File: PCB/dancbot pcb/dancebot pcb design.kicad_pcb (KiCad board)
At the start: 2 copper layers, 27 parts, among them J1 ESP32-PICO-KIT-V4.1, J2 Voltage Regulator, J4 Pins, J6 Conn_01x04_Socket, J7 Conn_01x04_Socket, Q1 PMOS, Q2 PMOS, Q3 2N3904, Q5 PMOS, SW1 SP switch, SW2 SW_SPST

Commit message: Layout Connections Revision 3
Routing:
- net +5V: track 97.9 -> 92.1 mm
- net GND1: track 3.71 -> 7.32 mm, vias 0 -> 2
- net SM4: track 18.5 -> 19.5 mm
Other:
- board outline added: 62.5 x 55 mm
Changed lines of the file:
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@@
     )
   )
-  (gr_rect (start 182 56) (end 251 121)
-    (stroke (width 0.2) (type default)) (fill none) (layer "F.Cu"))
+  (gr_rect (start 182.5 57.5) (end 245 112.5)
+    (stroke (width 0.1) (type default)) (fill none) (layer "Edge.Cuts"))
   (segment (start 197.92 63) (end 192.92 68) (width 0.25) (layer "F.Cu") (net 3))
   (segment (start 223.885 60.635) (end 224.73 61.48) (width 0.25) (layer "F.Cu") (net 3))
@@
   (segment (start 197.31104 98.5) (end 200.66 101.84896) (width 0.25) (layer "F.Cu") (net 6))
   (segment (start 237.5 62.46) (end 242.5 67.46) (width 0.25) (layer "F.Cu") (net 6))
-  (segment (start 192 101) (end 194.5 98.5) (width 0.25) (layer "F.Cu") (net 6))
   (segment (start 237.738 91.468) (end 237.738 95) (width 0.25) (layer "F.Cu") (net 6))
   (segment (start 242.5 67.46) (end 242.5 95) (width 0.25) (layer "F.Cu") (net 6))
@@
   (segment (start 242.5 95) (end 237.738 95) (width 0.25) (layer "F.Cu") (net 6))
   (segment (start 237.738 95.002) (end 236.22 96.52) (width 0.25) (layer "F.Cu") (net 6))
-  (segment (start 194.5 98.5) (end 196.71 98.5) (width 0.25) (layer "F.Cu") (net 6))
   (segment (start 200.66 103.23104) (end 203.10896 105.68) (width 0.25) (layer "F.Cu") (net 6))
   (segment (start 206.74 105.68) (end 203.71 105.68) (width 0.25) (layer "F.Cu") (net 6))
@@
   (segment (start 215.9 96.52) (end 208.28 104.14) (width 0.25) (layer "B.Cu") (net 6))
   (segment (start 236.22 96.52) (end 215.9 96.52) (width 0.25) (layer "B.Cu") (net 6))
-  (segment (start 217.418 105.387) (end 215.9 106.905) (width 0.25) (layer "F.Cu") (net 7))
-  (segment (start 217.418 91.468) (end 217.418 105.387) (width 0.25) (layer "F.Cu") (net 7))
-  (segment (start 219.958 91.468) (end 219.958 105.702) (width 0.25) (layer "F.Cu") (net 8))
-  (segment (start 219.958 105.702) (end 218.44 107.22) (width 0.25) (layer "F.Cu") (net 8))
+  (segment (start 215.9 92.986) (end 215.9 106.905) (width 0.25) (layer "F.Cu") (net 7))
+  (segment (start 217.418 91.468) (end 215.9 92.986) (width 0.25) (layer "F.Cu") (net 7))
+  (segment (start 219.958 91.468) (end 218.44 92.986) (width 0.25) (layer "F.Cu") (net 8))
+  (segment (start 218.44 92.986) (end 218.44 107.22) (width 0.25) (layer "F.Cu") (net 8))
   (segment (start 214.878 91.468) (end 213.36 92.986) (width 0.25) (layer "F.Cu") (net 9))
   (segment (start 213.36 92.986) (end 213.36 106.905) (width 0.25) (layer "F.Cu") (net 9))
-  (segment (start 220.98 92.986) (end 220.98 106.68) (width 0.25) (layer "F.Cu") (net 10))
-  (segment (start 221.3 107) (end 223.52 107) (width 0.25) (layer "F.Cu") (net 10))
-  (segment (start 220.98 106.68) (end 221.3 107) (width 0.25) (layer "F.Cu") (net 10))
-  (segment (start 222.498 91.468) (end 220.98 92.986) (width 0.25) (layer "F.Cu") (net 10))
+  (segment (start 220 106) (end 221 107) (width 0.25) (layer "F.Cu") (net 10))
+  (segment (start 221 107) (end 223.52 107) (width 0.25) (layer "F.Cu") (net 10))
+  (segment (start 220 93.966) (end 220 106) (width 0.25) (layer "F.Cu") (net 10))
+  (segment (start 222.498 91.468) (end 220 93.966) (width 0.25) (layer "F.Cu") (net 10))
   (segment (start 190 70) (end 185.675 74.325) (width 0.25) (layer "F.Cu") (net 11))
   (segment (start 207.5 107.5) (end 208 107) (width 0.25) (layer "F.Cu") (net 11))
@@
   (segment (start 222.6075 99.6875) (end 223.92 101) (width 0.25) (layer "F.Cu") (net 48))
   (segment (start 193 107.18) (end 196.71 107.18) (width 0.25) (layer "F.Cu") (net 49))
+  (segment (start 223.52 108) (end 225 106.52) (width 0.25) (layer "F.Cu") (net 49))
+  (segment (start 225 106.52) (end 225 106) (width 0.25) (layer "F.Cu") (net 49))
+  (via (at 225 106) (size 0.8) (drill 0.4) (layers "F.Cu" "B.Cu") (net 49))
+  (via (at 225 105) (size 0.8) (drill 0.4) (layers "F.Cu" "B.Cu") (net 49))
+  (segment (start 225 106) (end 225 105) (width 0.25) (layer "B.Cu") (net 49))
   (segment (start 215.486 68) (end 209.798 73.688) (width 0.25) (layer "F.Cu") (net 50))
   (segment (start 217 68) (end 215.486 68) (width 0.25) (layer "F.Cu") (net 50))
@@
     (polygon
       (pts
-        (xy 180 55)
-        (xy 253 55)
-        (xy 253 122)
-        (xy 180 122)
+        (xy 181 56)
+        (xy 181 115)
+        (xy 249 115)
+        (xy 249 56)
       )
     )

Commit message: Layout Connections Revision 4
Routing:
- net GND1: track 7.32 -> 37.2 mm, vias 2 -> 4
- net +5V: track 92.1 -> 88.4 mm
- net VOUT: track 57.1 -> 55.2 mm
- net Net-(R4-Pad1): track 50.3 -> 49.0 mm
- net SM5: track 75.8 -> 75.2 mm

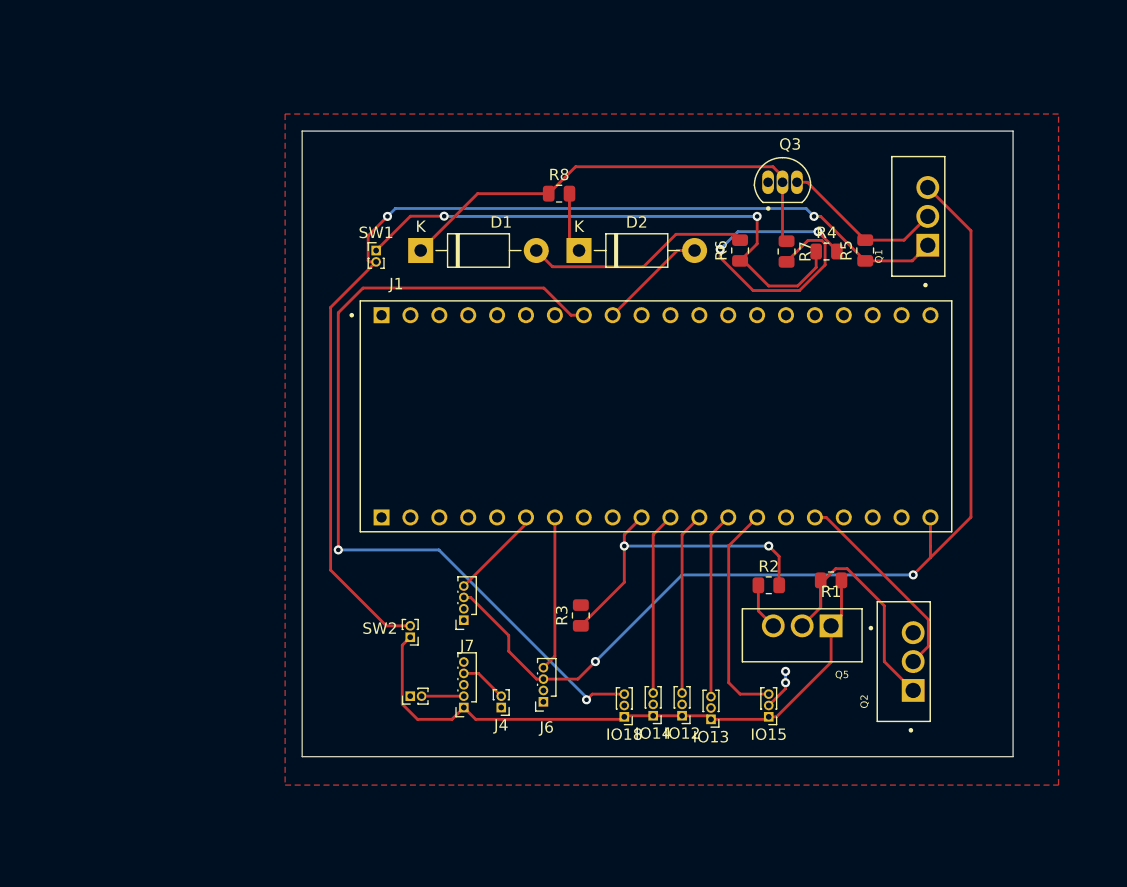
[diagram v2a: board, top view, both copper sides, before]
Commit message: Routing rev5, fixed batt lvl checker, fixed gnd plane
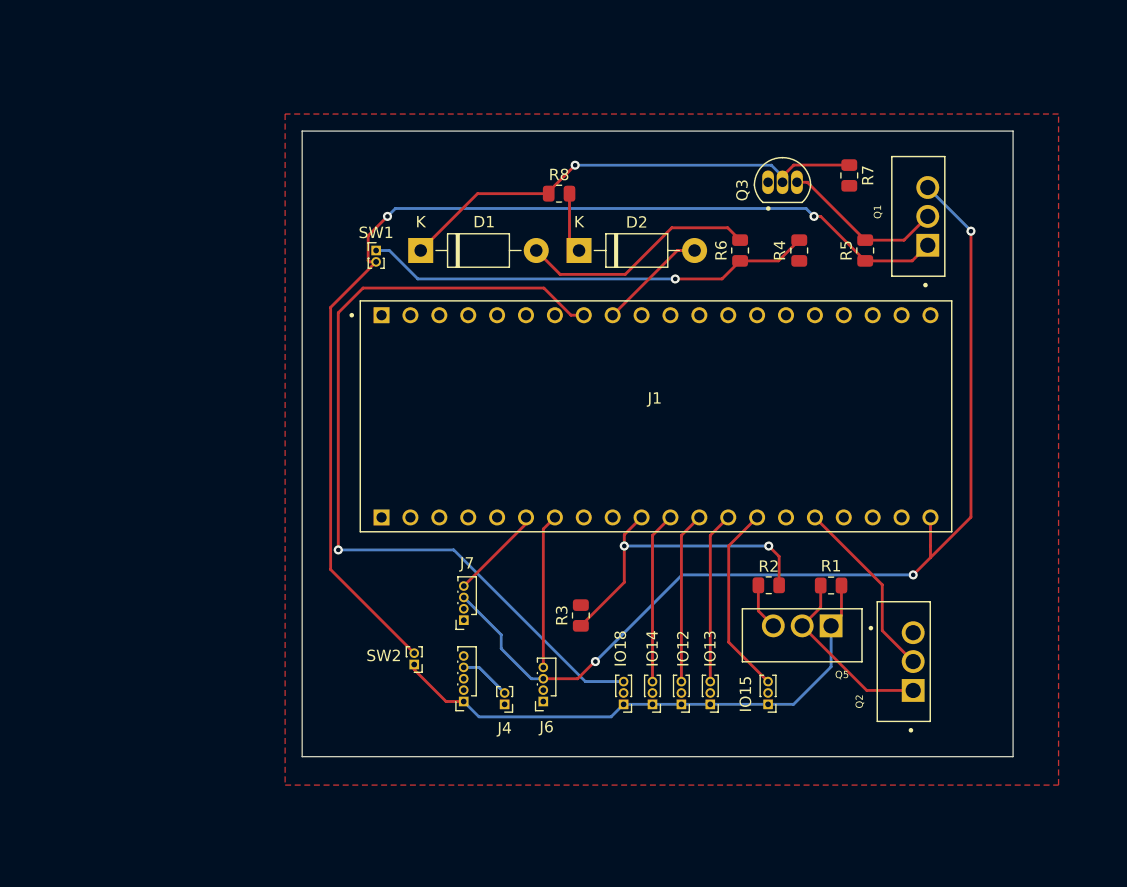
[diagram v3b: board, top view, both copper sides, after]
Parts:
- removed BT1: Battery, Connector_PinHeader_1.00mm:PinHeader_1x02_P1.00mm_Vertical
- moved R7 8.67 mm to (230.6, 61.4)
- moved SW2 2.43 mm to (192.3, 104.4)
- moved R4 2.40 mm to (226.2, 68.0), turned to -90 degrees
- moved IO13 1.32 mm to (218.4, 107.9)
- moved IO15 1.10 mm to (223.5, 107.9)
- moved IO18 1.10 mm to (210.8, 107.9)
- moved IO12 1.01 mm to (215.8, 107.9)
- moved IO14 1.01 mm to (213.3, 107.9)
- moved J2 0.53 mm to (196.7, 107.7)
- moved R1 0.45 mm to (229.0, 97.5)
- moved J4 0.41 mm to (200.3, 107.9)
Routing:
- net GND1: track 37.2 -> 0.00 mm, vias 4 -> 0
- net Net-(R4-Pad1): track 49.0 -> 39.6 mm, vias 2 -> 1
- net Net-(Q2-D): track 22.7 -> 16.3 mm
- net VOUT: track 55.2 -> 49.4 mm
- net SM4: track 19.5 -> 16.9 mm
- net Net-(D1-K): track 41.1 -> 42.8 mm, vias 0 -> 1
- net BATT EN: track 17.9 -> 16.3 mm
- net Net-(Q1-D): track 93.4 -> 94.7 mm
- net SM3: track 16.4 -> 15.1 mm
- net SM5: track 75.2 -> 74.2 mm, vias 2 -> 1
- net Net-(D1-A): track 19.9 -> 20.9 mm
- net SM2: track 16.1 -> 15.1 mm
- net SM1: track 16.1 -> 15.1 mm
- net +5V: track 88.4 -> 88.3 mm, vias 2 -> 3

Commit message: PCB size changed to 62x54mm
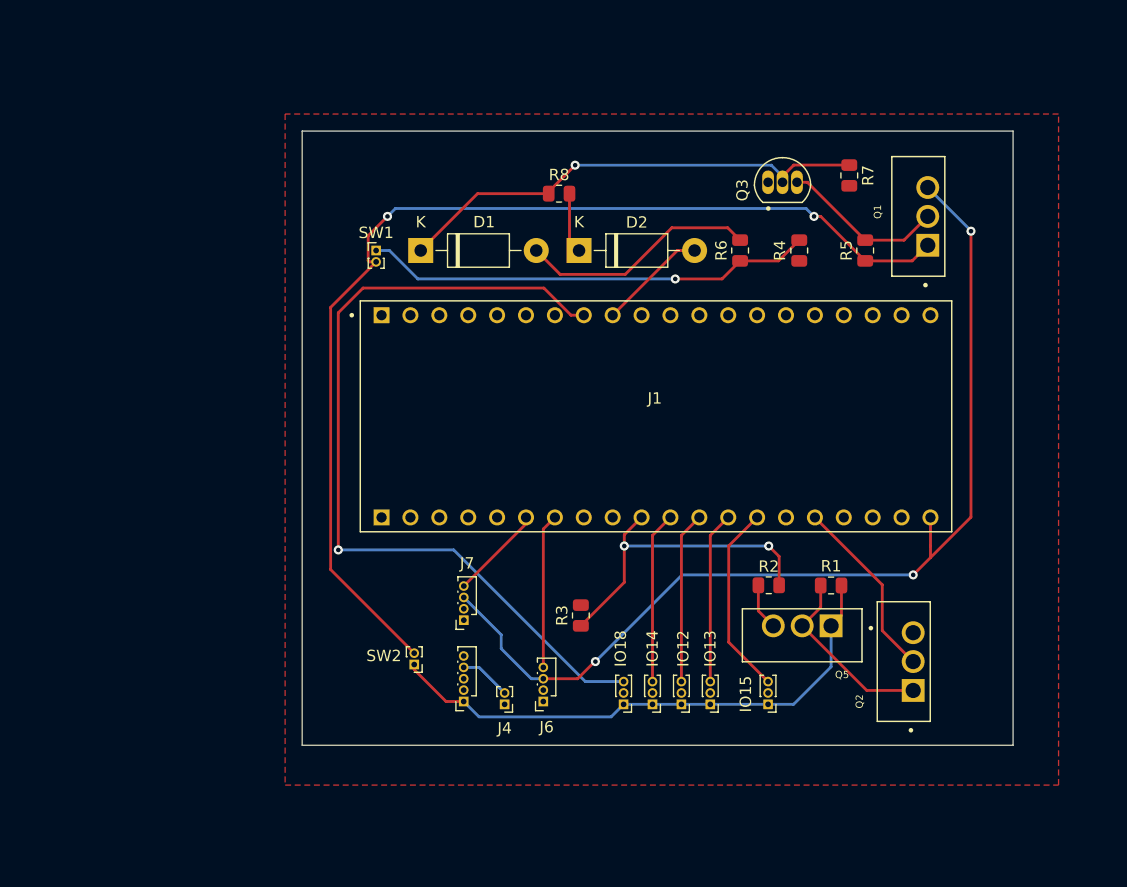
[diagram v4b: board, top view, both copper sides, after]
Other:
- board size 62.5 x 55 mm -> 62.5 x 54 mm
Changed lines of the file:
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@@
     )
   )
-  (gr_rect (start 182.5 57.5) (end 245 112.5)
+  (gr_rect (start 182.5 57.5) (end 245 111.5)
     (stroke (width 0.1) (type default)) (fill none) (layer "Edge.Cuts"))
   (segment (start 224.7 62.03) (end 224.73 62) (width 0.25) (layer "F.Cu") (net 2))

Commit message: Routing rev 6, trace width increased, smd components added
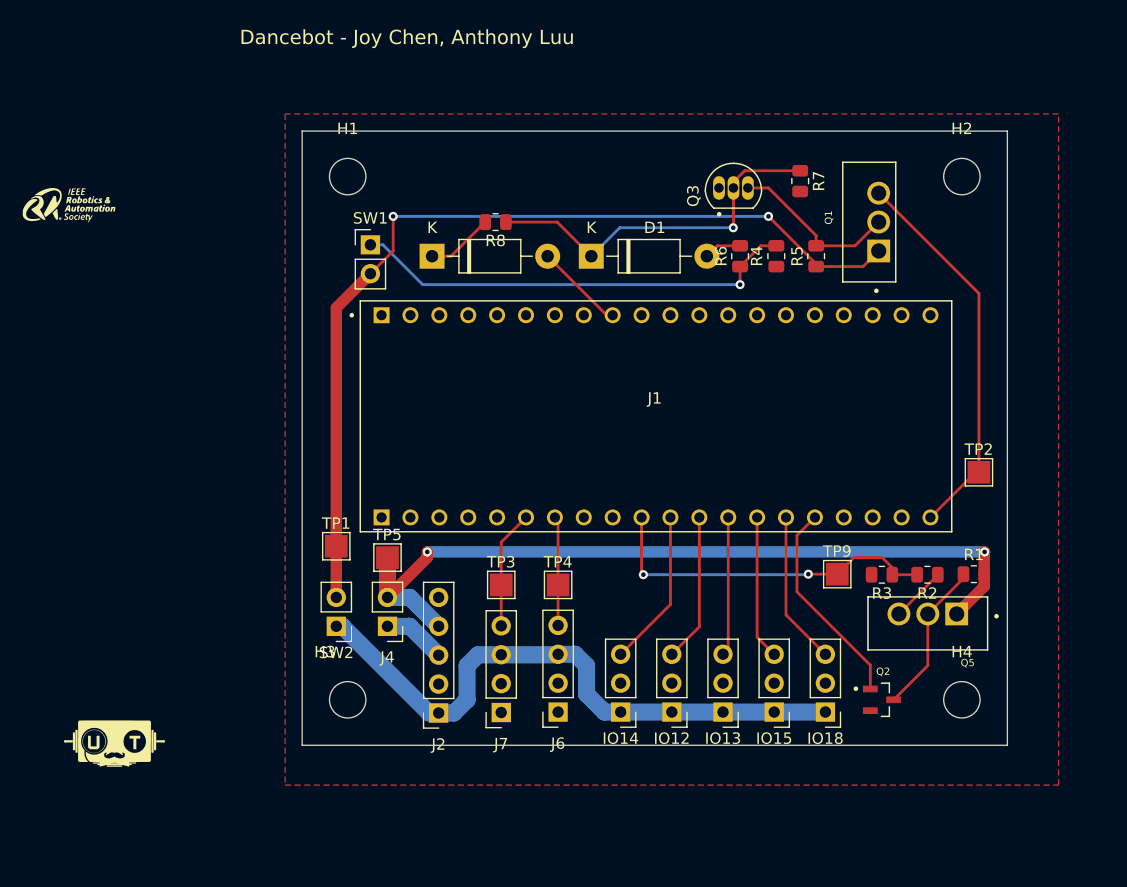
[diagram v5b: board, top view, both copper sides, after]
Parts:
- added G***: LOGO, LOGO, F.Cu at (162.0, 64.0)
- added G***: LOGO, LOGO, F.Cu at (166.0, 111.0)
- added H1: MountingHole, MountingHole:MountingHole_3.2mm_M3, F.Cu at (186.5, 61.5)
- added H2: MountingHole, MountingHole:MountingHole_3.2mm_M3, F.Cu at (240.5, 61.5)
- added H3: MountingHole, MountingHole:MountingHole_3.2mm_M3, F.Cu at (186.5, 107.5)
- added H4: MountingHole, MountingHole:MountingHole_3.2mm_M3, F.Cu at (240.5, 107.5)
- added TP1: TestPoint, TestPoint:TestPoint_Pad_2.0x2.0mm, F.Cu at (185.5, 94.0)
- added TP2: TestPoint, TestPoint:TestPoint_Pad_2.0x2.0mm, F.Cu at (242.0, 87.5)
- added TP3: TestPoint, TestPoint:TestPoint_Pad_2.0x2.0mm, F.Cu at (200.0, 97.4)
- added TP4: TestPoint, TestPoint:TestPoint_Pad_2.0x2.0mm, F.Cu at (205.0, 97.4)
- added TP5: TestPoint, TestPoint:TestPoint_Pad_2.0x2.0mm, F.Cu at (190.0, 95.0)
- added TP9: TestPoint, TestPoint:TestPoint_Pad_2.0x2.0mm, F.Cu at (229.5, 96.5)
- IO12, IO13, IO14, IO15, IO18: footprint Connector_PinHeader_1.00mm:PinHeader_1x03_P1.00mm_Vertical -> Connector_PinHeader_2.54mm:PinHeader_1x03_P2.54mm_Vertical
- J2: footprint Connector_PinSocket_1.00mm:PinSocket_1x05_P1.00mm_Vertical -> Connector_PinSocket_2.54mm:PinSocket_1x05_P2.54mm_Vertical
- J4, SW1, SW2: footprint Connector_PinHeader_1.00mm:PinHeader_1x02_P1.00mm_Vertical -> Connector_PinHeader_2.54mm:PinHeader_1x02_P2.54mm_Vertical
- J6, J7: footprint Connector_PinSocket_1.00mm:PinSocket_1x04_P1.00mm_Vertical -> Connector_PinSocket_2.54mm:PinSocket_1x04_P2.54mm_Vertical
- Q2: value PMOS -> NMOS; footprint dancebot pcb libraries stuff:TO254P1052X465X1989-3 -> Dancebot Footprints:SOT95P237X112-3N
- Q5: footprint dancebot pcb libraries stuff:TO254P1052X465X1989-3 -> Dancebot Footprints:TO254P1052X465X1989-3
- R3: value 10K -> 51k
- moved R3 26.7 mm to (233.5, 96.5), turned to 180 degrees
- moved IO18 17.8 mm to (228.5, 108.6)
- moved D1 15.0 mm to (207.9, 68.5)
- moved R2 14.0 mm to (237.5, 96.5), turned to 180 degrees
- moved D2 12.9 mm to (193.9, 68.5)
- moved R1 12.6 mm to (241.6, 96.5)
- moved J4 12.4 mm to (190.0, 101.0)
- moved Q5 11.1 mm to (240.0, 100.0)
- moved J7 8.76 mm to (200.0, 108.6)
- moved SW2 7.63 mm to (185.5, 101.0)
- moved R8 6.12 mm to (199.5, 65.5), turned to 180 degrees
- moved Q1 4.34 mm to (233.2, 68.0)
- moved Q3 4.34 mm to (220.4, 62.5)
- moved R5 4.34 mm to (227.7, 68.5)
- moved R7 4.34 mm to (226.3, 61.9)
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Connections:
- J1 pad J2_8: SM5 -> unconnected-(J1-IO18-PadJ2_8)
- J1 pad J3_15: unconnected-(J1-IO2-PadJ3_15) -> SM5
- J4 pad 1: GND1 -> Batt GND
- J6 pad 3: +5V -> VOUT
- J7 pad 3: +5V -> VOUT
- Q2 pad 1: Net-(Q2-D) -> BATT EN
- Q2 pad 2: BATT EN -> GND1
- Q2 pad 3: GND1 -> Net-(Q5-G)
- Q5 pad 1: VOUT -> Batt PWR
- Q5 pad 2: Net-(Q2-D) -> Net-(Q5-G)
- R1 pad 1: VOUT -> Batt PWR
- R1 pad 2: Net-(Q2-D) -> Net-(Q5-G)
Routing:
- net Batt PWR: track 4.53 -> 70.0 mm, vias 0 -> 2
- net SM5: track 74.2 -> 13.5 mm, vias 1 -> 0
- net +5V: track 88.3 -> 34.1 mm, vias 3 -> 0
- net Net-(D1-A): track 20.9 -> 3.30 mm
- net Net-(Q2-D): track 16.3 -> 0.00 mm
- net Net-(Q1-D): track 94.7 -> 80.8 mm
- net Net-(Q5-G): track 0.00 -> 13.6 mm
- net Net-(D1-K): track 42.8 -> 33.1 mm
- net Batt GND: track 0.00 -> 5.55 mm
- net VOUT: track 49.4 -> 53.6 mm
- net SM4: track 16.9 -> 12.7 mm
- net NPRightEye: track 13.6 -> 9.61 mm
- net SM3: track 15.1 -> 12.2 mm
- net NPLeftEye: track 8.30 -> 11.0 mm
- net BATT ADC: track 28.3 -> 30.8 mm
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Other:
- board size 62.5 x 54 mm -> 62 x 54 mm
- board text added: "Dancebot - Joy Chen, Anthony Luu"

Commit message: Routing rev6, swapped MOSFETs THT w/ SMD, fixed some clearence issues
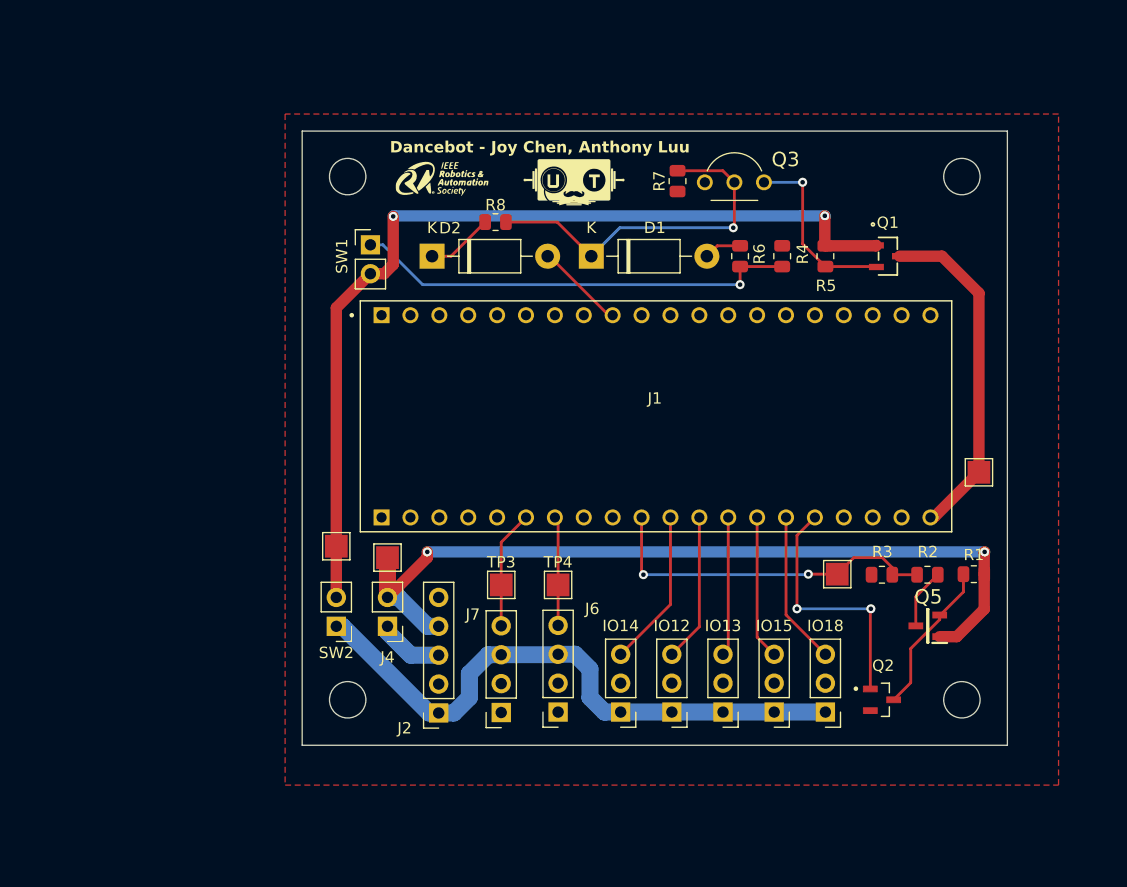
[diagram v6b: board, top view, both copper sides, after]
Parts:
- Q1: footprint dancebot pcb libraries stuff:TO254P1052X465X1989-3 -> Dancebot Footprints:SQ2351CES
- Q2: value NMOS -> IRLML2502TRPBF
- Q3: footprint 2N3904:TO92127P495H495-3 -> Dancebot Footprints:2N3904TFR
- Q5: value PMOS -> IRLML6402TRPBF; footprint Dancebot Footprints:TO254P1052X465X1989-3 -> Dancebot Footprints:IRLML6402TRPBF
- moved G*** 63.8 mm to (206.4, 61.6)
- moved G*** 32.9 mm to (194.8, 61.7)
- moved R7 10.8 mm to (215.5, 61.9)
- moved Q5 2.75 mm to (237.5, 101.0)
- moved Q3 2.56 mm to (217.9, 62.0), turned to 180 degrees
- moved Q1 0.93 mm to (234.0, 68.5), turned to -90 degrees
- moved R5 0.81 mm to (228.5, 68.5), turned to -90 degrees
- moved R4 0.51 mm to (224.7, 68.5), turned to 90 degrees
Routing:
- net BATT EN: track 18.4 -> 22.3 mm, vias 0 -> 2
- net +5V: track 34.1 -> 30.3 mm
- net Batt PWR: track 70.0 -> 73.5 mm
- net Net-(D1-K): track 33.1 -> 31.7 mm
- net Net-(Q1-G): track 15.0 -> 16.1 mm, vias 0 -> 1
- net Net-(Q1-D): track 80.8 -> 81.5 mm
- net Latch_Out: track 7.87 -> 8.40 mm
- net VOUT: track 53.6 -> 53.1 mm
